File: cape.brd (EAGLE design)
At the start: 100 x 80 mm, 30 parts

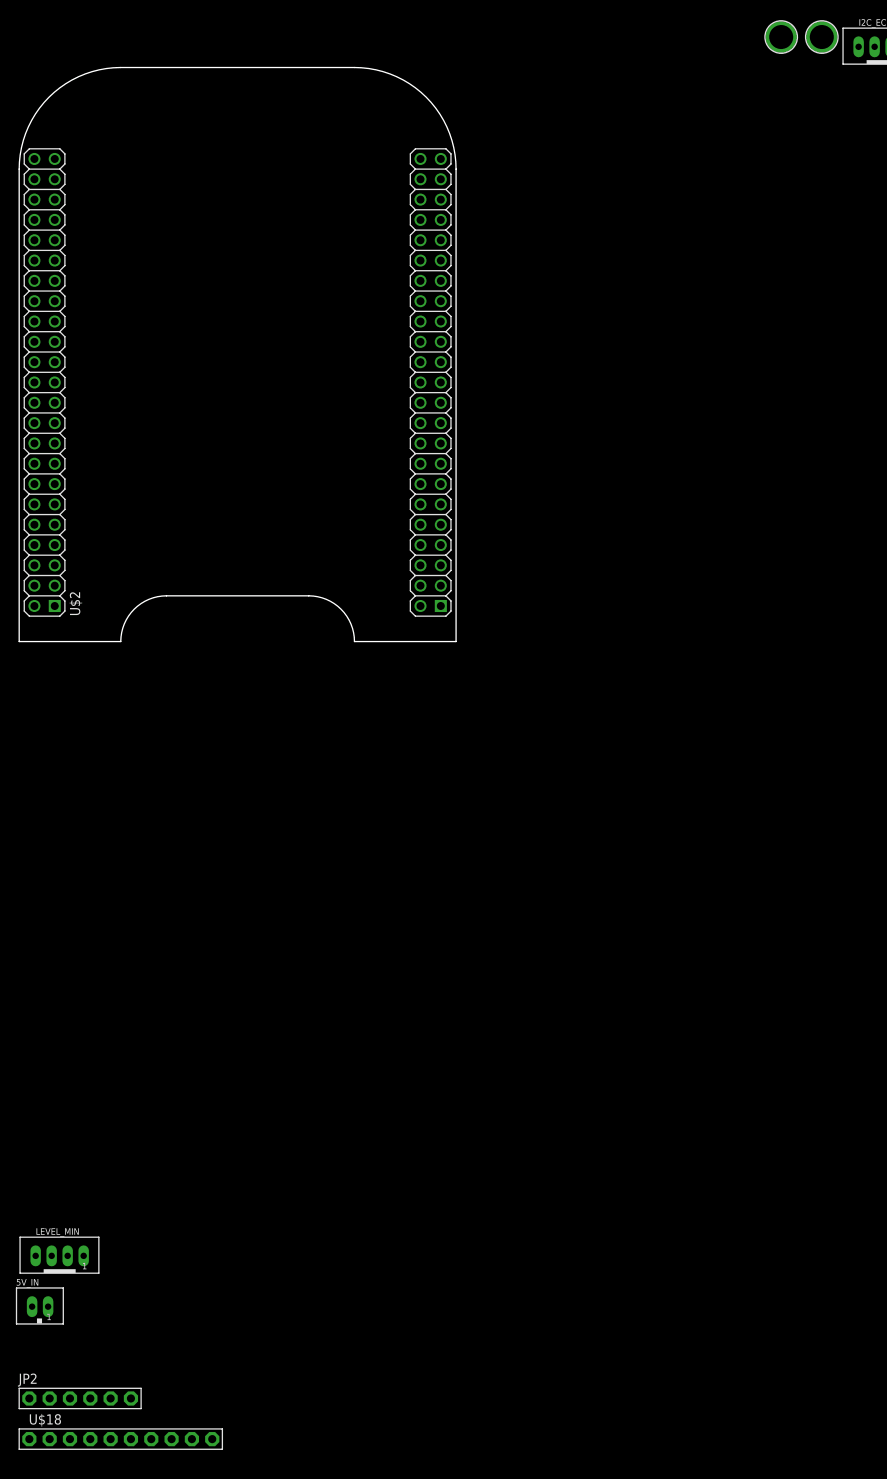
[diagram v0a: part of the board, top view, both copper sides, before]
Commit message: fix BB names int pinout
in the library adafruit
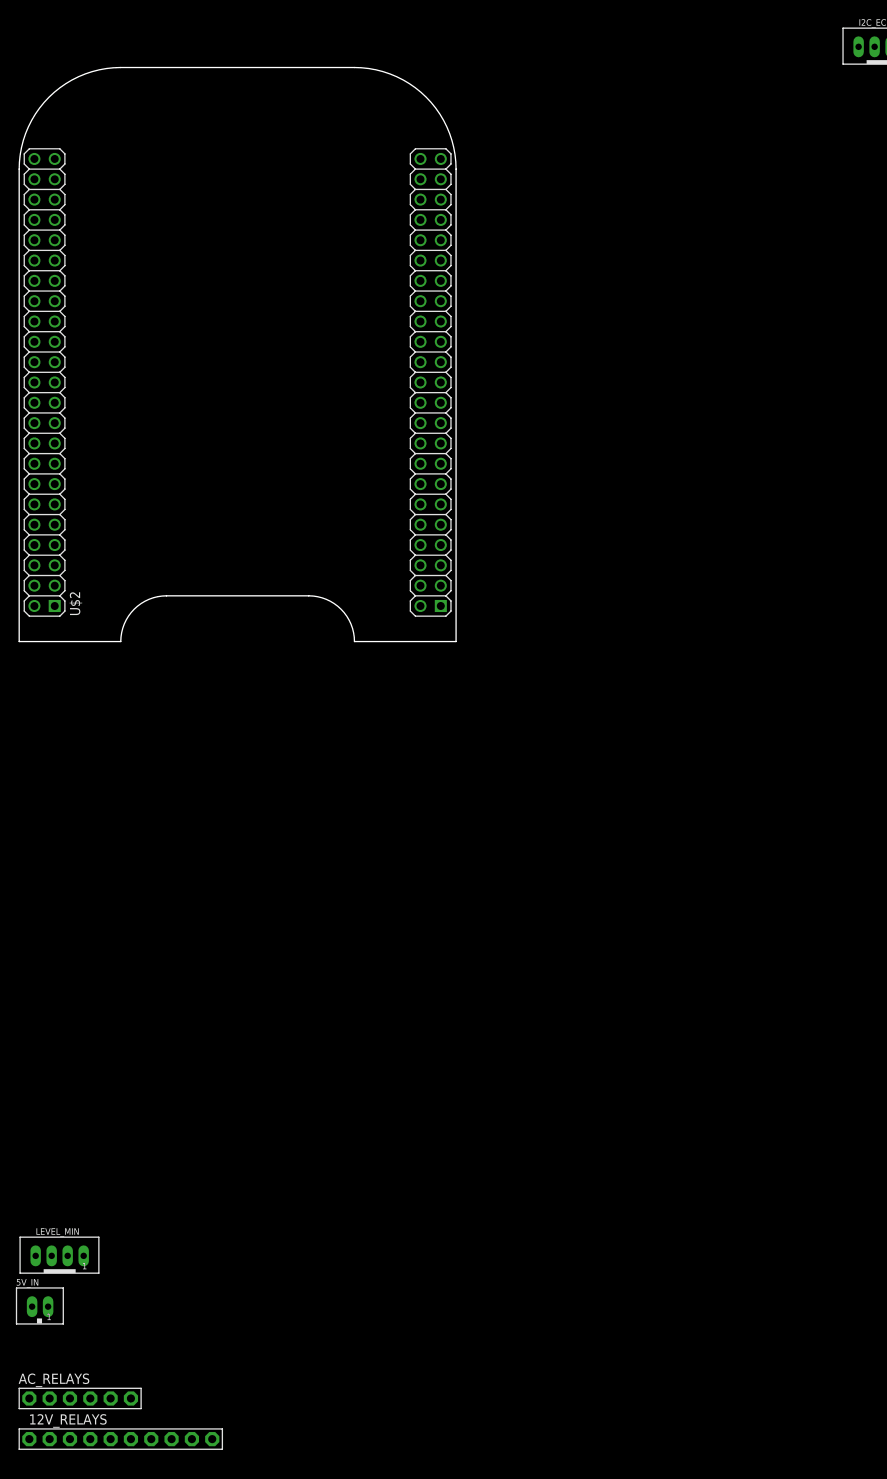
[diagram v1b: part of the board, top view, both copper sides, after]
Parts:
- removed U$22, U$23: MOUNTINGHOLE3.0THIN, microbuilder:MOUNTINGHOLE_3.0_PLATEDTHIN
- added FRAME1: FRAME-LEDGER, SparkFun-Aesthetics:CREATIVE_COMMONS
- renumbered JP2 to AC_RELAYS, U$18 to 12V_RELAYS
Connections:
- net GPIO_117 renamed LEVEL_MED
- net GPIO_20 renamed PH+
- net GPIO_48 renamed NUT3
- net GPIO_49 renamed NUT2
- net GPIO_50 renamed LEVEL_MAX
- net GPIO_51 renamed LEVEL_CW
- net GPIO_68 renamed PH-
- removed net GIPO_30: AC_RELAYS.5
- removed net GPIO_31: AC_RELAYS.4
- removed net GPIO_67: 12V_RELAYS.8
- removed net GPIO_69: 12V_RELAYS.9
- new net FAN: AC_RELAYS.2
- new net LEDS: AC_RELAYS.3
- new net LEVEL_MIN: LEVEL_MIN.P1, R1.2
- new net N$1: U$2.9
- new net NUT1: 12V_RELAYS.3
- new net WATER: 12V_RELAYS.2
- net GPIO_115: no longer LEVEL_MIN.P1, R1.2
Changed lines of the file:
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@@
 <element name="DHT22" library="SRG" package="JST_B4B-PH_HEADER" value="JST-PH_4-PIN_HEADER" x="-27.94" y="90.17"/>
 <element name="I2C_EC" library="SRG" package="JST_B4B-PH_HEADER" value="JST-PH_4-PIN_HEADER" x="-38.1" y="90.17"/>
-<element name="U$22" library="microbuilder" package="MOUNTINGHOLE_3.0_PLATEDTHIN" value="MOUNTINGHOLE3.0THIN" x="-45.72" y="91.44"/>
-<element name="U$23" library="microbuilder" package="MOUNTINGHOLE_3.0_PLATEDTHIN" value="MOUNTINGHOLE3.0THIN" x="-50.8" y="91.44"/>
 <element name="U$2" library="adafruit" package="BEAGLEBONE_SHIELD" value="BEAGLEBONE_OUTLINE" x="-146.05" y="1.27"/>
 <element name="LEVEL_MIN" library="SRG" package="JST_B4B-PH_HEADER" value="JST-PH_4-PIN_HEADER" x="-140.97" y="-60.96"/>
 <element name="5V_IN" library="SRG" package="JST_B2B-PH_HEADER" value="JST-PH_2-PIN_HEADER" x="-143.51" y="-67.31"/>
-<element name="JP2" library="adafruit" package="1X06-BIG" value="" x="-138.43" y="-78.74"/>
-<element name="U$18" library="adafruit" package="1X10-BIG" value="PINHD-1X10" x="-133.35" y="-83.82"/>
+<element name="AC_RELAYS" library="adafruit" package="1X06-BIG" value="" x="-138.43" y="-78.74"/>
+<element name="12V_RELAYS" library="adafruit" package="1X10-BIG" value="PINHD-1X10" x="-133.35" y="-83.82"/>
 <element name="R1" library="adafruit" package="R0805" value="" x="-144.78" y="-109.22"/>
 <element name="LEVEL_MED" library="SRG" package="JST_B4B-PH_HEADER" value="JST-PH_4-PIN_HEADER" x="-140.97" y="-114.3"/>
@@
 <element name="LEVEL_CW1" library="SRG" package="JST_B4B-PH_HEADER" value="JST-PH_4-PIN_HEADER" x="-140.97" y="-172.72"/>
 <element name="R12" library="adafruit" package="R0805" value="" x="-139.7" y="-196.85"/>
+<element name="FRAME1" library="SparkFun-Aesthetics" package="CREATIVE_COMMONS" value="FRAME-LEDGER" x="-125.73" y="-205.74"/>
 </elements>
 <signals>
 <signal name="GND">
+<contactref element="5V_IN" pad="P2"/>
+<contactref element="R1" pad="1"/>
+<contactref element="R2" pad="1"/>
+<contactref element="R3" pad="1"/>
+<contactref element="R4" pad="1"/>
+<contactref element="12V_RELAYS" pad="1"/>
+<contactref element="AC_RELAYS" pad="1"/>
+<contactref element="I2C_EC" pad="P2"/>
+<contactref element="I2C_PH" pad="P2"/>
+<contactref element="DHT22" pad="P1"/>
+<contactref element="DS18B20" pad="P1"/>
+<contactref element="R9" pad="1"/>
+<contactref element="R10" pad="1"/>
+<contactref element="R11" pad="1"/>
+<contactref element="R12" pad="1"/>
 <contactref element="U$2" pad="47"/>
 <contactref element="U$2" pad="48"/>
@@
 <contactref element="U$2" pad="1"/>
 <contactref element="U$2" pad="2"/>
-<contactref element="5V_IN" pad="P2"/>
-<contactref element="R1" pad="1"/>
-<contactref element="R2" pad="1"/>
-<contactref element="R3" pad="1"/>
-<contactref element="R4" pad="1"/>
-<contactref element="U$18" pad="1"/>
-<contactref element="JP2" pad="1"/>
-<contactref element="I2C_EC" pad="P2"/>
-<contactref element="I2C_PH" pad="P2"/>
-<contactref element="DHT22" pad="P1"/>
-<contactref element="DS18B20" pad="P1"/>
-<contactref element="R9" pad="1"/>
-<contactref element="R10" pad="1"/>
-<contactref element="R11" pad="1"/>
-<contactref element="R12" pad="1"/>
 <wire x1="-144.78" y1="-78.74" x2="-144.78" y2="-83.82" width="0" layer="19" extent="1-1"/>
 <wire x1="-144.435" y1="-67.2625" x2="-144.78" y2="-78.74" width="0" layer="19" extent="1-1"/>
@@
 <contactref element="LEVEL_MAX" pad="P4"/>
 <contactref element="LEVEL_CW" pad="P4"/>
-<contactref element="U$18" pad="10"/>
-<contactref element="JP2" pad="6"/>
+<contactref element="12V_RELAYS" pad="10"/>
+<contactref element="AC_RELAYS" pad="6"/>
 <contactref element="R5" pad="2"/>
 <contactref element="R6" pad="2"/>
@@
 <signal name="GPIO_115">
 <contactref element="U$2" pad="15"/>
-<contactref element="R1" pad="2"/>
-<contactref element="LEVEL_MIN" pad="P1"/>
-<wire x1="-137.99" y1="-60.9125" x2="-143.78" y2="-109.22" width="0" layer="19" extent="1-1"/>
-<wire x1="-141.605" y1="38.1" x2="-137.99" y2="-60.9125" width="0" layer="19" extent="1-1"/>
-</signal>
-<signal name="GPIO_117">
+</signal>
+<signal name="LEVEL_MED">
 <contactref element="R2" pad="2"/>
 <contactref element="LEVEL_MED" pad="P1"/>
 <wire x1="-143.78" y1="-119.38" x2="-137.99" y2="-114.2525" width="0" layer="19" extent="1-1"/>
 </signal>
-<signal name="GPIO_50">
+<signal name="LEVEL_MAX">
 <contactref element="R3" pad="2"/>
 <contactref element="LEVEL_MAX" pad="P1"/>
 <wire x1="-137.99" y1="-124.4125" x2="-143.78" y2="-135.89" width="0" layer="19" extent="1-1"/>
 </signal>
-<signal name="GPIO_51">
+<signal name="LEVEL_CW">
 <contactref element="R4" pad="2"/>
 <contactref element="LEVEL_CW" pad="P1"/>
 <wire x1="-137.99" y1="-130.7625" x2="-138.7" y2="-135.89" width="0" layer="19" extent="1-1"/>
 </signal>
-<signal name="GPIO_69">
-<contactref element="U$18" pad="9"/>
-</signal>
-<signal name="GPIO_67">
-<contactref element="U$18" pad="8"/>
-</signal>
-<signal name="GPIO_68">
-<contactref element="U$18" pad="7"/>
-</signal>
-<signal name="GPIO_20">
-<contactref element="U$18" pad="6"/>
-</signal>
-<signal name="GPIO_48">
-<contactref element="U$18" pad="5"/>
-</signal>
-<signal name="GPIO_49">
-<contactref element="U$18" pad="4"/>
-</signal>
-<signal name="GIPO_30">
-<contactref element="JP2" pad="5"/>
-</signal>
-<signal name="GPIO_31">
-<contactref element="JP2" pad="4"/>
+<signal name="NUT2">
+<contactref element="12V_RELAYS" pad="4"/>
+</signal>
+<signal name="NUT3">
+<contactref element="12V_RELAYS" pad="5"/>
 </signal>
 <signal name="SCL">
@@
 <wire x1="-137.99" y1="-172.6725" x2="-138.7" y2="-196.85" width="0" layer="19" extent="1-1"/>
 </signal>
+<signal name="LEVEL_MIN">
+<contactref element="R1" pad="2"/>
+<contactref element="LEVEL_MIN" pad="P1"/>
+<wire x1="-137.99" y1="-60.9125" x2="-143.78" y2="-109.22" width="0" layer="19" extent="1-1"/>
+</signal>
+<signal name="WATER">
+<contactref element="12V_RELAYS" pad="2"/>
+</signal>
+<signal name="NUT1">
+<contactref element="12V_RELAYS" pad="3"/>
+</signal>
+<signal name="PH+">
+<contactref element="12V_RELAYS" pad="6"/>
+</signal>
+<signal name="PH-">
+<contactref element="12V_RELAYS" pad="7"/>
+</signal>
+<signal name="FAN">
+<contactref element="AC_RELAYS" pad="2"/>
+</signal>
+<signal name="LEDS">
+<contactref element="AC_RELAYS" pad="3"/>
+</signal>
+<signal name="N$1">
+<contactref element="U$2" pad="9"/>
+</signal>
 </signals>

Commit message: change conectors to smd
and add 4 relays
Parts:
- removed 5V_IN: JST-PH_2-PIN_HEADER, SRG:JST_B2B-PH_HEADER
- removed DHT22, I2C_EC, I2C_PH, LEVEL_CW1, LEVEL_MAX1, LEVEL_MED, LEVEL_MED1, LEVEL_MIN1: JST-PH_4-PIN_HEADER, SRG:JST_B4B-PH_HEADER
- added +5V: BM02B-SRSS-TB, con-jst:BM02B-SRSS-TB
- added DHT, EC, GPIO, LDR, LEVE_MED, MUSIC, ON/OFF, PH: BM04B-SRSS-TB, con-jst:BM04B-SRSS-TB
- added Q1: MOSFET-NCHANNELBSS123LT1G, SparkFun-DiscreteSemi:SOT23-3
- added R13: 4.7K, adafruit:R0805
- added R14, R15: 10K, adafruit:R0805
- added U$1, U$3: FIDUCIAL, adafruit:FIDUCIAL_1MM
- DS18B20, LEVEL_CW, LEVEL_MAX, LEVEL_MIN: value JST-PH_4-PIN_HEADER -> BM04B-SRSS-TB; device SRG:JST_B4B-PH_HEADER -> con-jst:BM04B-SRSS-TB
- R1, R10, R11, R12, R2, R3, R4, R9: value (none) -> 10K
- R5, R6, R8: value 4k7 -> 4.7K
- R7: value 4k7 -> 100
- moved R12 322.2 mm to (72.4, 45.7), turned to 90 degrees
- moved R11 318.9 mm to (62.2, 45.7), turned to 90 degrees
- moved R10 300.3 mm to (52.1, 45.7), turned to 90 degrees
- moved R9 300.0 mm to (41.9, 45.7), turned to 90 degrees
- moved R8 288.7 mm to (72.6, 36.8), turned to 180 degrees
- moved R7 286.5 mm to (62.2, 39.4), turned to 90 degrees
- moved R4 285.9 mm to (72.4, 55.9), turned to 90 degrees
- moved DS18B20 283.8 mm to (57.1, 36.8), turned to 90 degrees
- moved R3 282.1 mm to (62.1, 55.9), turned to 90 degrees
- moved LEVEL_CW 279.7 mm to (67.3, 55.9), turned to 90 degrees
- moved R6 268.7 mm to (52.1, 36.8), turned to 270 degrees
- moved LEVEL_MAX 267.9 mm to (57.1, 55.9), turned to 90 degrees
- moved R2 263.6 mm to (52.1, 55.9), turned to 90 degrees
- moved FRAME1 257.6 mm to (29.2, 0.00)
- moved R5 256.9 mm to (41.9, 36.8), turned to 270 degrees
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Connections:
- removed net GPIO_115: U$2.15
- removed net VDD_3V3EXP: U$2.49, U$2.50
- new net 12V_1: 12V_RELAYS.8, U$2.71
- new net 12V_2: 12V_RELAYS.9, U$2.88
- new net AC_1: AC_RELAYS.4, U$2.60
- new net AC_2: AC_RELAYS.5, U$2.73
- new net LEVE_CW: LEVEL_CW.4
- new net N1: DS18B20.1, R13.1, R7.1
- new net VDD_3V3: DS18B20.4, EC.4, GPIO.4, LDR.4, MUSIC.4, ON/OFF.4, PH.4, R1.1, R10.1, R11.1, R12.1, R13.2, R15.2, R2.1, R3.1, R4.1, R5.2, R6.2, R9.1, U$2.49, U$2.50
- net DHT_AM2302: now also Q1.2, R15.1, U$2.68; no longer DHT22.P3
- net DIGITAL_LDR: now also LDR.1, U$2.7; no longer LEVEL_MIN1.P1
- net DS18B20: now also R7.2, U$2.67; no longer DS18B20.P3
- net FAN: now also U$2.59
- net GND: now also +5V.1, DHT.3, DS18B20.3, EC.3, GPIO.3, LDR.3, LEVEL_MAX.4, LEVEL_MIN.4, LEVE_MED.4, MUSIC.3, ON/OFF.3, PH.3; no longer 5V_IN.P2, DHT22.P1, DS18B20.P1, I2C_EC.P2, I2C_PH.P2, R1.1, R10.1, R11.1, R12.1, R2.1, R3.1, R4.1, R9.1
- net GPIO: now also GPIO.1, U$2.27; no longer LEVEL_CW1.P1
- net LEDS: now also U$2.57
- net LEVEL_CW: now also LEVEL_CW.1, U$2.33; no longer LEVEL_CW.P1
- net LEVEL_MAX: now also LEVEL_MAX.1, U$2.30; no longer LEVEL_MAX.P1
- net LEVEL_MED: now also LEVE_MED.1, U$2.34; no longer LEVEL_MED.P1
- net LEVEL_MIN: now also LEVEL_MIN.1, U$2.32; no longer LEVEL_MIN.P1
- net MUSIC: now also MUSIC.1, U$2.19; no longer LEVEL_MAX1.P1
- net N$1: now also DHT.1, Q1.3, R14.1, R8.1; no longer U$2.9
- net NUT1: now also U$2.8
- net NUT2: now also U$2.10
- net NUT3: now also U$2.87
- net ON/OFF: now also ON/OFF.1, U$2.13; no longer LEVEL_MED1.P1
- net PH+: now also U$2.61
- net PH-: now also U$2.70
- net SCL: now also EC.1, PH.1, R6.1; no longer I2C_EC.P4, I2C_PH.P4, R5.1, R7.1
- net SDA: now also EC.2, PH.2, R5.1; no longer I2C_EC.P3, I2C_PH.P3, R6.1, R8.1
- net VCC: now also +5V.2, DHT.4, Q1.1, R14.2; no longer 5V_IN.P1, DHT22.P4, DS18B20.P4, I2C_EC.P1, I2C_PH.P1, LEVEL_CW.P4, LEVEL_CW1.P4, LEVEL_MAX.P4, LEVEL_MAX1.P4, LEVEL_MED.P4, LEVEL_MED1.P4, LEVEL_MIN.P4, LEVEL_MIN1.P4, R5.2, R6.2, R7.2
- net WATER: now also U$2.9
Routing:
- net VDD_3V3: track 0.00 -> 209.0 mm, vias 0 -> 2
- net VCC: track 0.00 -> 69.0 mm, vias 0 -> 3
- net NUT1: track 0.00 -> 52.3 mm, vias 0 -> 2
- net WATER: track 0.00 -> 50.5 mm, vias 0 -> 1
- net GND: track 0.00 -> 49.4 mm
- net NUT2: track 0.00 -> 49.2 mm
- net DHT_AM2302: track 0.00 -> 43.4 mm, vias 0 -> 1
- net DS18B20: track 0.00 -> 40.3 mm, vias 0 -> 1
- net LEVEL_MIN: track 0.00 -> 35.3 mm, vias 0 -> 2
- net NUT3: track 0.00 -> 34.2 mm, vias 0 -> 1
- net DIGITAL_LDR: track 0.00 -> 25.2 mm, vias 0 -> 1
- net GPIO: track 0.00 -> 24.9 mm, vias 0 -> 1
- net LEVEL_MED: track 0.00 -> 24.5 mm, vias 0 -> 1
- net MUSIC: track 0.00 -> 24.1 mm, vias 0 -> 1
- net 12V_2: track 0.00 -> 23.6 mm, vias 0 -> 1
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- added copper zone on layer 1, net GND
- added copper zone on layer 16, net GND
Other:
- board size 100 x 80 mm -> 71.8 x 54.6 mm
